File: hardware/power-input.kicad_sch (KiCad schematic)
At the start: 2 parts, among them J1 USB_C_Receptacle_USB2.0_14P, U2 USBLC6-2SC6

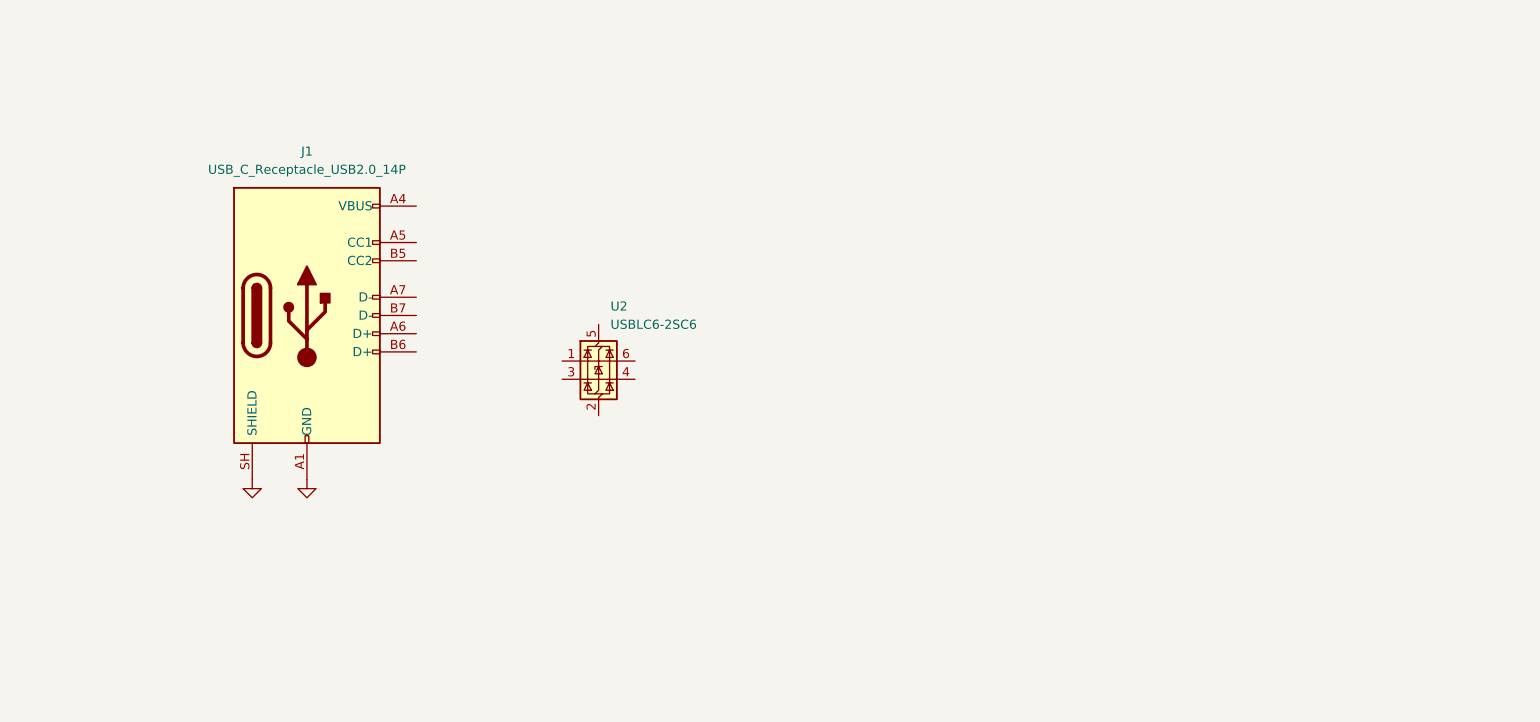
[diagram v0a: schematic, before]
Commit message: Draft power inputs sheet
Added USB C PD input and external supply, with ideal diode ORing.
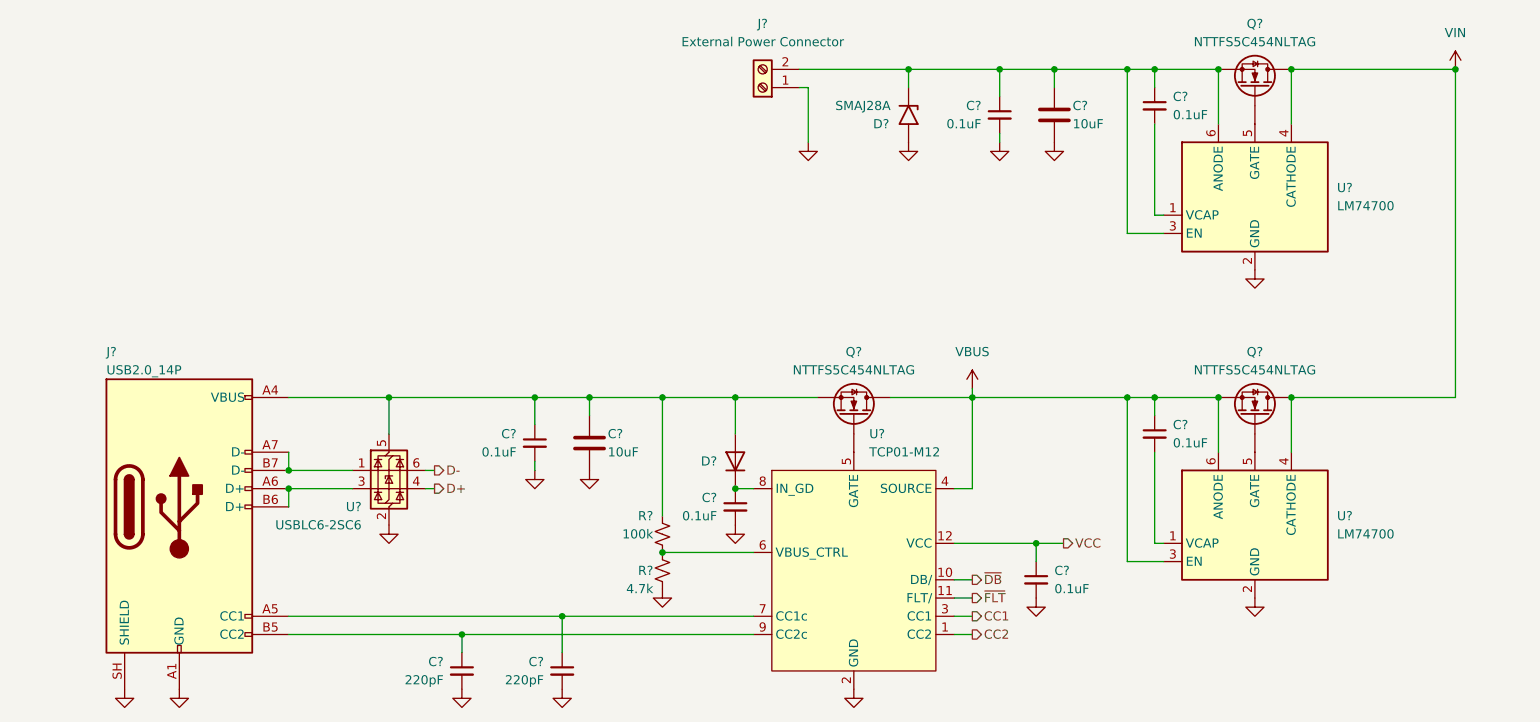
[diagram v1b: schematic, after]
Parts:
- added C? (x6): 0.1uF, Capacitor_SMD:C_0603_1608Metric_Pad1.08x0.95mm_HandSolder, symbol Device:C_Small
- added C? (x2): 220pF, Capacitor_SMD:C_0603_1608Metric_Pad1.08x0.95mm_HandSolder, symbol Device:C_Small
- added C? (x2): 10uF, symbol Device:C
- added D?: SMAJ28A, Diode_SMD:D_SMA, symbol Diode:SMAJ28A
- added D?: RB751V-40, Diode_SMD:D_SOD-323_HandSoldering, symbol Device:D
- added J?: External Power Connector, TerminalBlock_CUI:TerminalBlock_CUI_TB007-508-02_1x02_P5.08mm_Horizontal, symbol Connector:Screw_Terminal_01x02
- added Q? (x3): NTTFS5C454NLTAG, stepping-stone:WDFN8_511AB_ONS_OSI, symbol stepping-stone:NTTFS5C454NLTAG
- added R?: 4.7k, symbol Device:R_Small_US
- added R?: 100k, symbol Device:R_Small_US
- added U? (x2): LM74700, Package_TO_SOT_SMD:SOT-23-6, symbol Power_Management:LM74700
- added U?: TCP01-M12, Package_DFN_QFN:QFN-12-1EP_3x3mm_P0.5mm_EP1.45x1.45mm, symbol stepping-stone:TCPP01-M12
- J?: renamed from J1; value USB_C_Receptacle_USB2.0_14P -> USB2.0_14P
- renumbered U2 to U?
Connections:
- net GND: now also U?.2 (GND), C?.2, C?.2, C?.2, C?.2, C?.2, C?.2, C?.2, C?.2, D?.2 (A2), J?.1 (Pin_1), R?.2, U?.13 (PAD), U?.2 (GND), U?.2 (GND), U?.2 (GND)
- net at U?.1 (I/O1): now also J?.A7 (D-), J?.B7 (D-)
- net at U?.3 (I/O2): now also J?.A6 (D+), J?.B6 (D+)
- net D+: now reaches U?.4 (I/O2)
- net at U?.5 (VBUS): now also J?.A4 (VBUS), J?.A9 (VBUS), J?.B4 (VBUS), J?.B9 (VBUS), C?.1, C?.1, D?.2 (A), Q?.[1,2,3] (S), R?.1
- net D-: now reaches U?.6 (I/O1)
- net at J?.A5 (CC1): now also C?.1, U?.7 (CC1c)
- net at J?.B5 (CC2): now also C?.1, U?.9 (CC2c)
- new net: C?.1, C?.1, C?.1, D?.1 (A1), J?.2 (Pin_2), Q?.[1,2,3] (S), U?.3 (EN), U?.6 (ANODE)
- new net: C?.1, D?.1 (K), U?.8 (IN_GD)
- new net: Q?.4 (G), U?.5 (GATE) (x3)
- new net: R?.1, R?.2, U?.6 (VBUS_CTRL)
- new net: C?.2, U?.1 (VCAP) (x2)
- new net CC1: U?.3 (CC1)
- new net CC2: U?.1 (CC2)
- new net VBUS: C?.1, Q?.[1,2,3] (S), Q?.[5,6,7,8] (D), U?.3 (EN), U?.4 (SOURCE), U?.6 (ANODE)
- new net VCC: C?.1, U?.12 (VCC)
- new net VIN: Q?.[5,6,7,8] (D), Q?.[5,6,7,8] (D), U?.4 (CATHODE), U?.4 (CATHODE)
- new net ~{DB}: U?.10 (DB/)
- new net ~{FLT}: U?.11 (FLT/)
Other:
- company: (none) -> Jacob Wigent
- title: (none) -> Power Input
- moved on the sheet: J?, U?

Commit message: Finalize source select
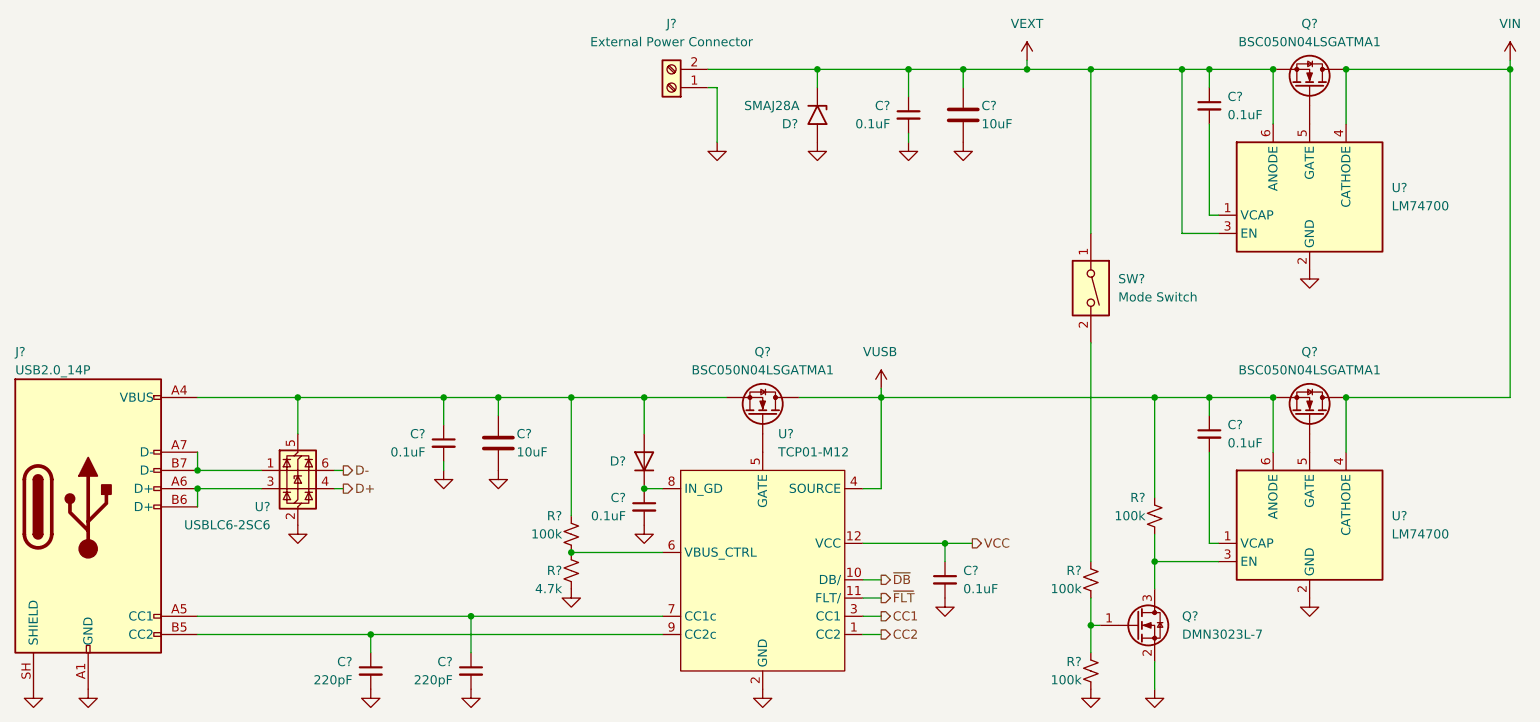
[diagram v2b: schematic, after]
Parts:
- removed C?: 10uF, symbol Device:C
- removed C?: 220pF, Capacitor_SMD:C_0603_1608Metric_Pad1.08x0.95mm_HandSolder, symbol Device:C_Small
- removed Q? (x3): NTTFS5C454NLTAG, stepping-stone:WDFN8_511AB_ONS_OSI, symbol stepping-stone:NTTFS5C454NLTAG
- removed U?: LM74700, Package_TO_SOT_SMD:SOT-23-6, symbol Power_Management:LM74700
- added C?: 220pF, Capacitor_SMD:C_0603_1608Metric_Pad1.08x0.95mm_HandSolder, symbol Device:C_Small
- added C?: 10uF, Capacitor_SMD:C_1210_3225Metric_Pad1.33x2.70mm_HandSolder, symbol Device:C
- added Q? (x3): BSC050N04LSGATMA1, Package_SON:Infineon_PG-TDSON-8_6.15x5.15mm, symbol stepping-stone:BSC050N04LSGATMA1
- added Q?: DMN3023L-7, Package_TO_SOT_SMD:SOT-23, symbol stepping-stone:DMN3023L-7
- added R? (x3): 100k, symbol Device:R_Small_US
- added SW?: Mode Switch, Button_Switch_SMD:SW_DIP_SPSTx01_Slide_9.78x4.72mm_W8.61mm_P2.54mm, symbol Switch:SW_DIP_x01
- added U?: LM74700, Package_TO_SOT_SMD:SOT-23-6, symbol Power_Management:LM74700
- C?: Part Number (none) -> C0603C221K5RACTU; Vendor URL (none) -> https://www.digikey.com/en/products/detail/kemet/C0603C221K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
- C?: footprint (none) -> Capacitor_SMD:C_1210_3225Metric_Pad1.33x2.70mm_HandSolder; Part Number (none) -> CL32B106KBJNNNE; Vendor URL (none) -> https://www.digikey.com/en/products/detail/samsung-electro-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
- U?: Part Number (none) -> LM74700QDBVTQ1; Vendor URL (none) -> https://www.digikey.com/en/products/detail/texas-instrument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
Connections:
- net GND: now also C?.2, C?.2, Q?.2 (S), R?.2, U?.2 (GND)
- net VIN: now also Q?.[5,6,7,8] (D), Q?.[5,6,7,8] (D), U?.4 (CATHODE)
- net VEXT: now reaches C?.1, C?.1, D?.1 (A1), J?.2 (Pin_2), U?.3 (EN), U?.6 (ANODE)
- net VEXT: now also C?.1, Q?.[1,2,3] (S), SW?.1
- net at U?.5 (GATE): now also Q?.4 (G) (x2)
- net at C?.1, C?.1, D?.2 (A)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: now also Q?.[1,2,3] (S)
- net at J?.A5 (CC1), U?.7 (CC1c): now also C?.1
- net at C?.2: now also U?.1 (VCAP)
- net VBUS renamed VUSB
- net VUSB: now also Q?.[1,2,3] (S), Q?.[5,6,7,8] (D), R?.1, U?.6 (ANODE)
- new net: Q?.1 (G), R?.1, R?.2
- new net: R?.1, SW?.2
- new net: Q?.4 (G), U?.5 (GATE)
- new net: Q?.3 (D), R?.2, U?.3 (EN)
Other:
- moved on the sheet: C?, D?, J?, R?, U?

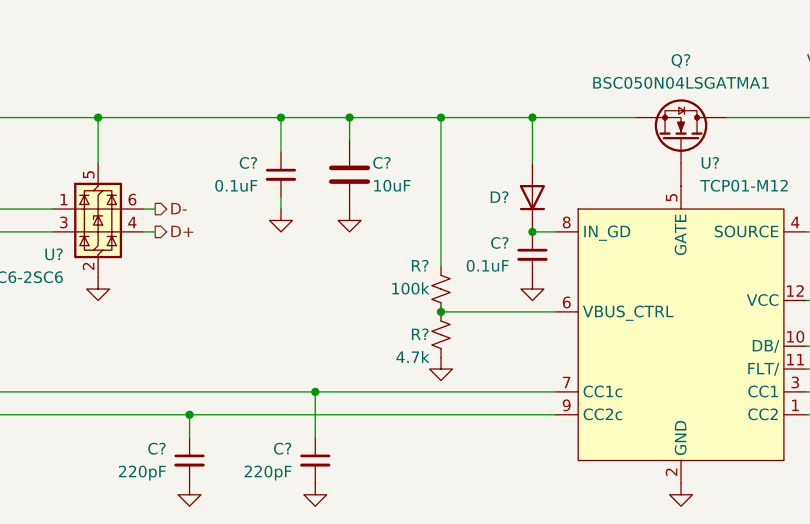
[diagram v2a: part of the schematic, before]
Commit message: Add 3.3V buck converter
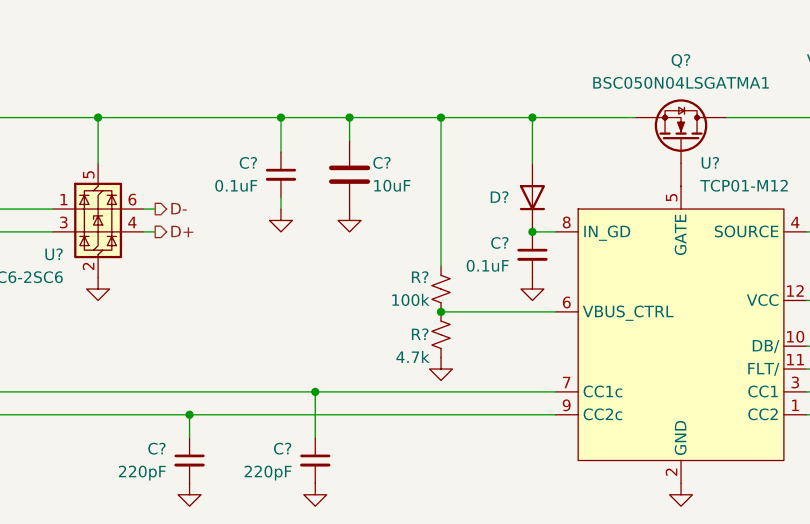
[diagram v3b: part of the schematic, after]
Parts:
- removed R? (x2): 100k, symbol Device:R_Small_US
- added R? (x2): 100k, Resistor_SMD:R_0603_1608Metric_Pad0.98x0.95mm_HandSolder, symbol Device:R_Small_US
- R?: footprint (none) -> Resistor_SMD:R_0603_1608Metric_Pad0.98x0.95mm_HandSolder; Part Number (none) -> RC0603FR-07100KL; Vendor URL (none) -> https://www.digikey.com/en/products/detail/yageo/RC0603FR-0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
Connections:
- net GND: now also R?.2
- net at Q?.1 (G), R?.2: now also R?.1
- net at R?.1, U?.6 (VBUS_CTRL): now also R?.2
- net at C?.1, C?.1, D?.2 (A)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: now also R?.1
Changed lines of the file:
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@@
 	)
 	(junction
-		(at 96.52 135.89)
+		(at 110.49 127)
 		(diameter 0)
 		(color 0 0 0 0)
 	)
 	(junction
-		(at 144.78 59.69)
+		(at 96.52 135.89)
 		(diameter 0)
 		(color 0 0 0 0)
 	)
 	(junction
-		(at 120.65 118.11)
+		(at 144.78 59.69)
 		(diameter 0)
 		(color 0 0 0 0)
 	)
 	(junction
-		(at 110.49 127)
+		(at 120.65 118.11)
 		(diameter 0)
 		(color 0 0 0 0)
@@
 	)
 	(symbol
-		(lib_id "Device:R_Small_US")
-		(at 182.88 143.51 0)
-		(unit 1)
-		(body_style 1)
-		(exclude_from_sim no)
-		(in_bom yes)
-		(on_board yes)
-		(in_pos_files yes)
-		(dnp no)
-		(property "Reference" "R?"
-			(at 181.61 142.24 0)
-			(show_name no)
-			(do_not_autoplace no)
-			(effects
-				(font
-					(size 1.27 1.27)
-				)
-				(justify right)
-			)
-		)
-		(property "Value" "100k"
-			(at 181.61 144.78 0)
-			(show_name no)
-			(do_not_autoplace no)
-			(effects
-				(font
-					(size 1.27 1.27)
-				)
-				(justify right)
-			)
-		)
-		(property "Footprint" ""
-			(at 182.88 143.51 0)
-			(hide yes)
-			(show_name no)
-			(do_not_autoplace no)
-			(effects
-				(font
-					(size 1.27 1.27)
-				)
-			)
-		)
-		(property "Datasheet" ""
-			(at 182.88 143.51 0)
-			(hide yes)
-			(show_name no)
-			(do_not_autoplace no)
-			(effects
-				(font
-					(size 1.27 1.27)
-				)
-			)
-		)
-		(property "Description" "Resistor, small US symbol"
-			(at 182.88 143.51 0)
-			(hide yes)
-			(show_name no)
-			(do_not_autoplace no)
-			(effects
-				(font
-					(size 1.27 1.27)
-				)
-			)
-		)
-		(pin "1"
-		)
-		(pin "2"
-		)
-		(instances
-			(project "stepping-stone"
-				(path "/793a882e-3f7b-468b-a863-41a1f527e1bf/73c4e66b-e11c-48b6-b2c8-fbbf612d64c5"
-					(reference "R?")
-					(unit 1)
-				)
-			)
-		)
-	)
-	(symbol
 		(lib_id "Device:C_Small")
 		(at 162.56 130.81 0)
@@
 			)
 		)
-		(property "Footprint" ""
+		(property "Footprint" "Resistor_SMD:R_0603_1608Metric_Pad0.98x0.95mm_HandSolder"
 			(at 182.88 130.81 0)
 			(hide yes)
@@
 			)
 		)
-		(property "Datasheet" ""
+		(property "Datasheet" "https://yageogroup.com/content/datasheet/asset/file/PYU-RC_GROUP_51_ROHS_L"
 			(at 182.88 130.81 0)
 			(hide yes)
@@
 			)
 		)
+		(property "Part Number" "RC0603FR-07100KL"
+			(at 182.88 130.81 0)
+			(hide yes)
+			(show_name no)
+			(do_not_autoplace no)
+			(effects
+				(font
+					(size 1.27 1.27)
+				)
+			)
+		)
+		(property "Vendor URL" "https://www.digikey.com/en/products/detail/yageo/RC0603FR-07100KL/726889"
+			(at 182.88 130.81 0)
+			(hide yes)
+			(show_name no)
+			(do_not_autoplace no)
+			(effects
+				(font
+					(size 1.27 1.27)
+				)
+			)
+		)
 		(pin "1"
 		)
@@
 	)
 	(symbol
+		(lib_id "Device:R_Small_US")
+		(at 110.49 124.46 0)
+		(unit 1)
+		(body_style 1)
+		(exclude_from_sim no)
+		(in_bom yes)
+		(on_board yes)
+		(in_pos_files yes)
+		(dnp no)
+		(property "Reference" "R?"
+			(at 109.22 123.19 0)
+			(show_name no)
+			(do_not_autoplace no)
+			(effects
+				(font
+					(size 1.27 1.27)
+				)
+				(justify right)
+			)
+		)
+		(property "Value" "100k"
+			(at 109.22 125.73 0)
+			(show_name no)
+			(do_not_autoplace no)
+			(effects
+				(font
+					(size 1.27 1.27)
+				)
+				(justify right)
+			)
+		)
+		(property "Footprint" "Resistor_SMD:R_0603_1608Metric_Pad0.98x0.95mm_HandSolder"
+			(at 110.49 124.46 0)
+			(hide yes)
+			(show_name no)
+			(do_not_autoplace no)
+			(effects
+				(font
+					(size 1.27 1.27)
+				)
+			)
+		)
+		(property "Datasheet" "https://yageogroup.com/content/datasheet/asset/file/PYU-RC_GROUP_51_ROHS_L"
+			(at 110.49 124.46 0)
+			(hide yes)
+			(show_name no)
+			(do_not_autoplace no)
+			(effects
+				(font
+					(size 1.27 1.27)
+				)
+			)
+		)
+		(property "Description" "Resistor, small US symbol"
+			(at 110.49 124.46 0)
+			(hide yes)
+			(show_name no)
+			(do_not_autoplace no)
+			(effects
+				(font
+					(size 1.27 1.27)
+				)
+			)
+		)
+		(property "Part Number" "RC0603FR-07100KL"
+			(at 110.49 124.46 0)
+			(hide yes)
+			(show_name no)
+			(do_not_autoplace no)
+			(effects
+				(font
+					(size 1.27 1.27)
+				)
+			)
+		)
+		(property "Vendor URL" "https://www.digikey.com/en/products/detail/yageo/RC0603FR-07100KL/726889"
+			(at 110.49 124.46 0)
+			(hide yes)
+			(show_name no)
+			(do_not_autoplace no)
+			(effects
+				(font
+					(size 1.27 1.27)
+				)
+			)
+		)
+		(pin "1"
+		)
+		(pin "2"
+		)
+		(instances
+			(project "stepping-stone"
+				(path "/793a882e-3f7b-468b-a863-41a1f527e1bf/73c4e66b-e11c-48b6-b2c8-fbbf612d64c5"
+					(reference "R?")
+					(unit 1)
+				)
+			)
+		)
+	)
+	(symbol
 		(lib_id "power:GND")
 		(at 96.52 146.05 0)
@@
 	)
 	(symbol
+		(lib_id "Device:R_Small_US")
+		(at 182.88 143.51 0)
+		(unit 1)
+		(body_style 1)
+		(exclude_from_sim no)
+		(in_bom yes)
+		(on_board yes)
+		(in_pos_files yes)
+		(dnp no)
+		(property "Reference" "R?"
+			(at 181.61 142.24 0)
+			(show_name no)
+			(do_not_autoplace no)
+			(effects
+				(font
+					(size 1.27 1.27)
+				)
+				(justify right)
+			)
+		)
+		(property "Value" "100k"
+			(at 181.61 144.78 0)
+			(show_name no)
+			(do_not_autoplace no)
+			(effects
+				(font
+					(size 1.27 1.27)
+				)
+				(justify right)
+			)
+		)
+		(property "Footprint" "Resistor_SMD:R_0603_1608Metric_Pad0.98x0.95mm_HandSolder"
+			(at 182.88 143.51 0)
+			(hide yes)
+			(show_name no)
+			(do_not_autoplace no)
+			(effects
+				(font
+					(size 1.27 1.27)
+				)
+			)
+		)
+		(property "Datasheet" "https://yageogroup.com/content/datasheet/asset/file/PYU-RC_GROUP_51_ROHS_L"
+			(at 182.88 143.51 0)
+			(hide yes)
+			(show_name no)
+			(do_not_autoplace no)
+			(effects
+				(font
+					(size 1.27 1.27)
+				)
+			)
+		)
+		(property "Description" "Resistor, small US symbol"
+			(at 182.88 143.51 0)
+			(hide yes)
+			(show_name no)
+			(do_not_autoplace no)
+			(effects
+				(font
+					(size 1.27 1.27)
+				)
+			)
+		)
+		(property "Part Number" "RC0603FR-07100KL"
+			(at 182.88 143.51 0)
+			(hide yes)
+			(show_name no)
+			(do_not_autoplace no)
+			(effects
+				(font
+					(size 1.27 1.27)
+				)
+			)
+		)
+		(property "Vendor URL" "https://www.digikey.com/en/products/detail/yageo/RC0603FR-07100KL/726889"
+			(at 182.88 143.51 0)
+			(hide yes)
+			(show_name no)
+			(do_not_autoplace no)
+			(effects
+				(font
+					(size 1.27 1.27)
+				)
+			)
+		)
+		(pin "1"
+		)
+		(pin "2"
+		)
+		(instances
+			(project "stepping-stone"
+				(path "/793a882e-3f7b-468b-a863-41a1f527e1bf/73c4e66b-e11c-48b6-b2c8-fbbf612d64c5"
+					(reference "R?")
+					(unit 1)
+				)
+			)
+		)
+	)
+	(symbol
 		(lib_id "power:GND")
 		(at 92.71 115.57 0)
@@
 					(unit 1)
 				)
-			)
-		)
-	)
-	(symbol
-		(lib_id "Device:R_Small_US")
-		(at 110.49 124.46 0)
-		(unit 1)
-		(body_style 1)
-		(exclude_from_sim no)
-		(in_bom yes)
-		(on_board yes)
-		(in_pos_files yes)
-		(dnp no)
-		(property "Reference" "R?"
-			(at 109.22 121.92 0)
-			(show_name no)
-			(do_not_autoplace no)
-			(effects
-				(font
-					(size 1.27 1.27)
-				)
-				(justify right)
-			)
-		)
-		(property "Value" "100k"
-			(at 109.22 124.46 0)
-			(show_name no)
-			(do_not_autoplace no)
-			(effects
-				(font
-					(size 1.27 1.27)
-				)
-				(justify right)
-			)
-		)
-		(property "Footprint" ""
-			(at 110.49 124.46 0)
-			(hide yes)
-			(show_name no)
-			(do_not_autoplace no)
-			(effects
-				(font
-					(size 1.27 1.27)
-				)
-			)
-		)
-		(property "Datasheet" ""
-			(at 110.49 124.46 0)
-			(hide yes)
-			(show_name no)
-			(do_not_autoplace no)
-			(effects
-				(font
-					(size 1.27 1.27)
-				)
-			)
-		)
-		(property "Description" "Resistor, small US symbol"
-			(at 110.49 124.46 0)
-			(hide yes)
-			(show_name no)
-			(do_not_autoplace no)
-			(effects
-				(font
-					(size 1.27 1.27)
-				)
-			)
-		)
-		(pin "1"
-		)
-		(pin "2"
-		)
-		(instances
-			(project "stepping-stone"
-				(path "/793a882e-3f7b-468b-a863-41a1f527e1bf/73c4e66b-e11c-48b6-b2c8-fbbf612d64c5"
-					(reference "R?")
-					(unit 1)
-				)
